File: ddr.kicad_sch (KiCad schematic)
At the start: 79 parts, among them U801 MT41K256M16TW

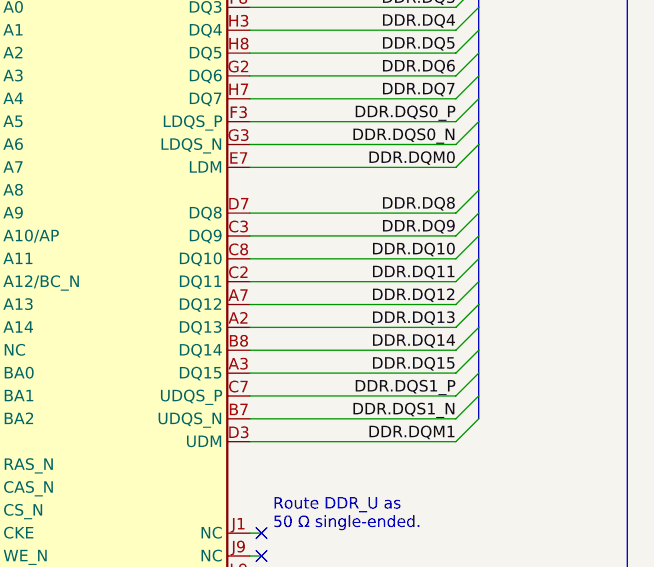
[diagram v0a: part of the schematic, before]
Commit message: Redo MPU fanout as dog-bone
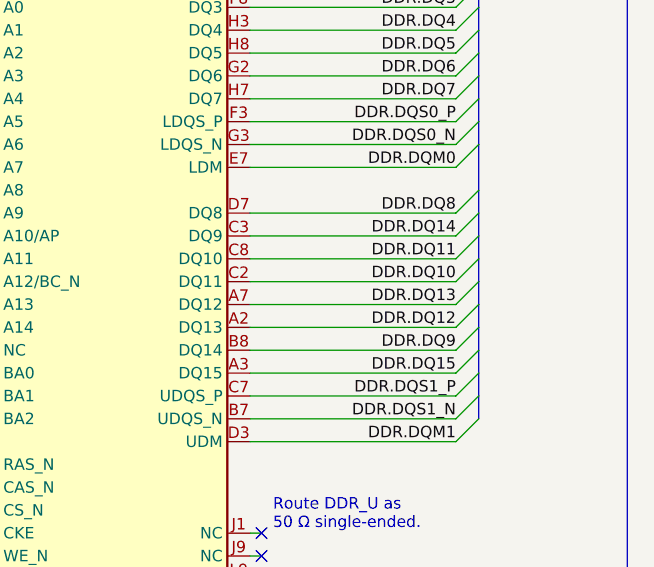
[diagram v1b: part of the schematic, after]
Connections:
- net DDR.DQ10: now also U801.C2 (DQ11); no longer U801.C8 (DQ10)
- net DDR.DQ11: now also U801.C8 (DQ10); no longer U801.C2 (DQ11)
- net DDR.DQ12: now also U801.A2 (DQ13); no longer U801.A7 (DQ12)
- net DDR.DQ13: now also U801.A7 (DQ12); no longer U801.A2 (DQ13)
- net DDR.DQ14: now also U801.C3 (DQ9); no longer U801.B8 (DQ14)
- net DDR.DQ9: now also U801.B8 (DQ14); no longer U801.C3 (DQ9)
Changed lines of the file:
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@@
 	)
 	(label "DDR.DQ13"
-		(at 387.35 142.24 180)
+		(at 387.35 139.7 180)
 		(effects
 			(font
@@
 	)
 	(label "DDR.DQ12"
-		(at 387.35 139.7 180)
+		(at 387.35 142.24 180)
 		(effects
 			(font
@@
 	)
 	(label "DDR.DQ14"
+		(at 387.35 132.08 180)
+		(effects
+			(font
+				(size 1.27 1.27)
+			)
+			(justify right bottom)
+		)
+	)
+	(label "DDR.DQ9"
 		(at 387.35 144.78 180)
-		(effects
-			(font
-				(size 1.27 1.27)
-			)
-			(justify right bottom)
-		)
-	)
-	(label "DDR.DQ9"
-		(at 387.35 132.08 180)
 		(effects
 			(font
@@
 	)
 	(label "DDR.DQ11"
-		(at 387.35 137.16 180)
+		(at 387.35 134.62 180)
 		(effects
 			(font
@@
 	)
 	(label "DDR.DQ10"
-		(at 387.35 134.62 180)
-		(effects
-			(font
+		(at 387.35 137.16 180)
+		(effects
+			(font

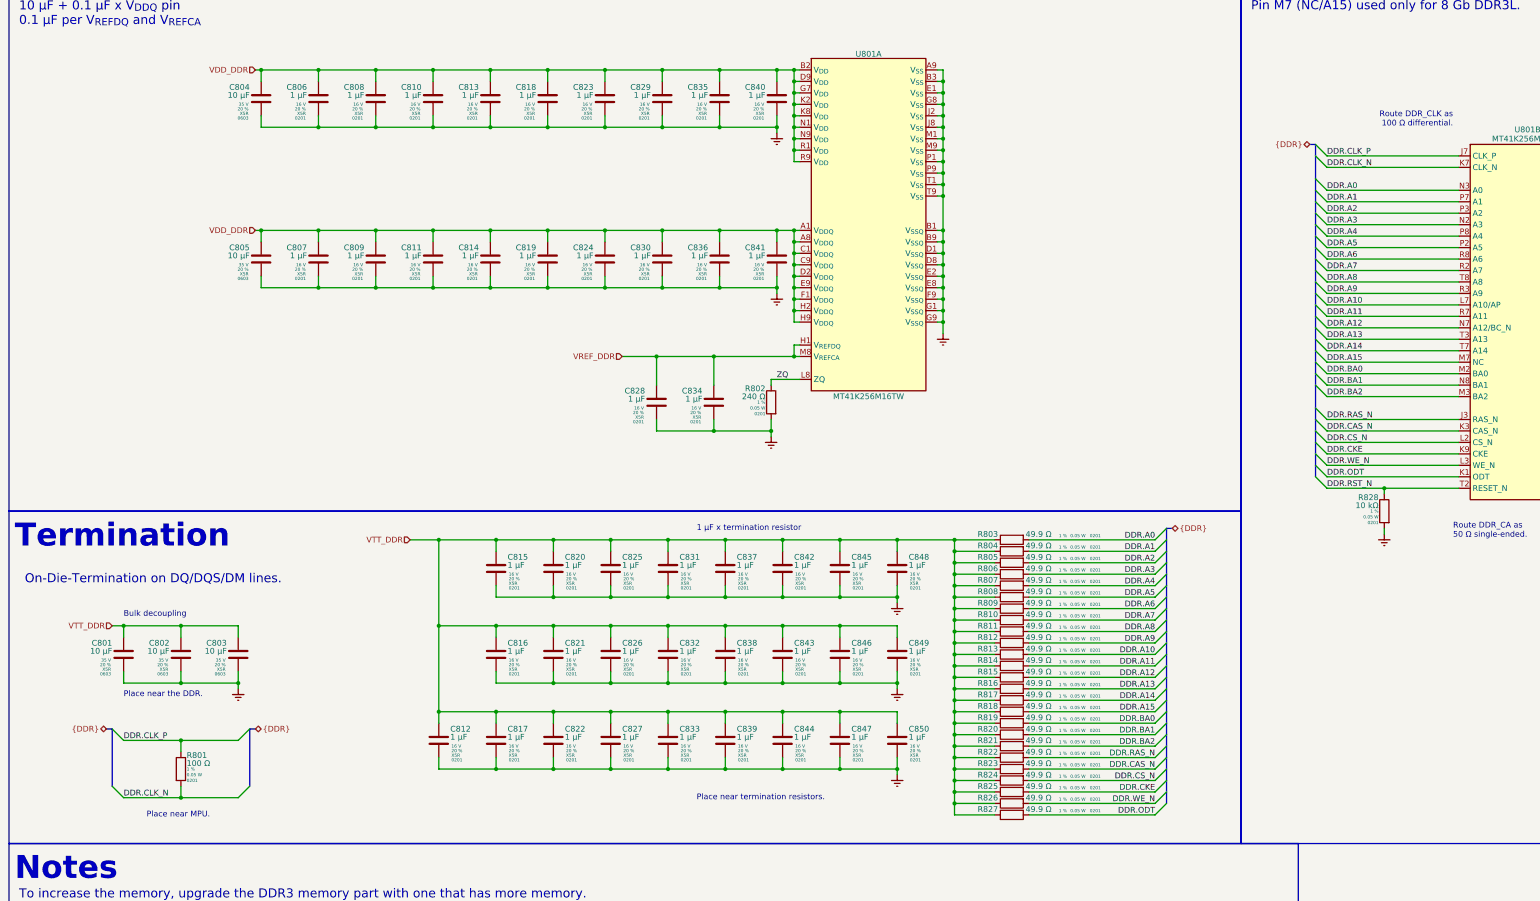
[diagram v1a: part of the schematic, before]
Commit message: Reorganize DDR termination
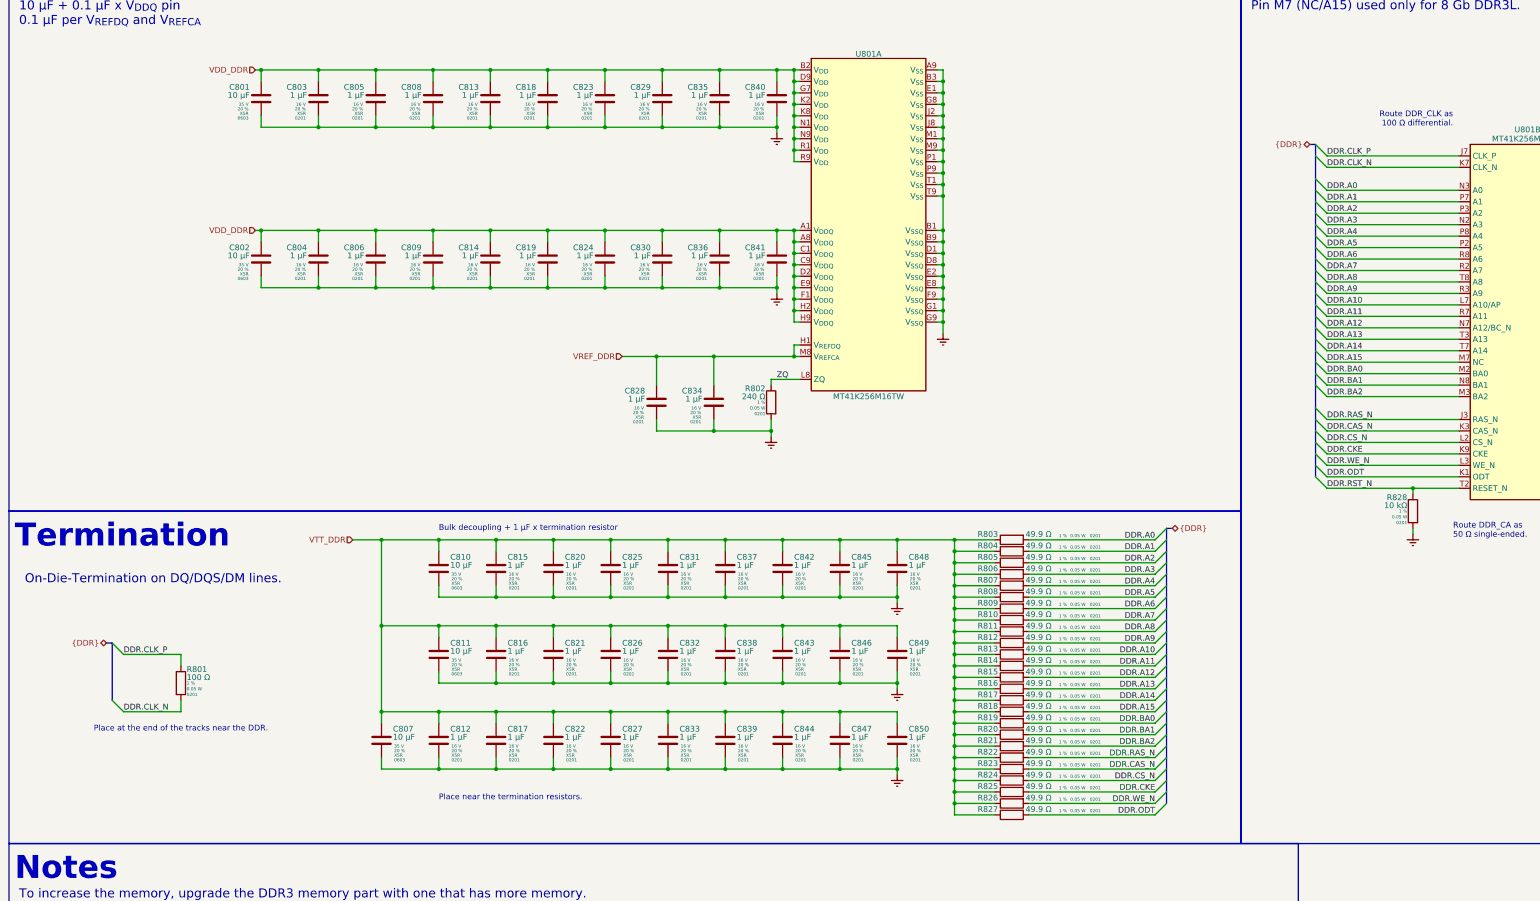
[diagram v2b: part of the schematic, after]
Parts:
- renumbered C804 to C801, C805 to C802, C806 to C803, C807 to C804, C808 to C805, C809 to C806, C803 to C807, C810 to C808, C811 to C809, C801 to C810, C802 to C811
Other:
- note added: "Bulk decoupling + 1 µF x termination resistor"
- note added: "Place at the end of the tracks near the DDR."
- note added: "Place near the termination resistors."
- note removed: "1 µF x termination resistor"
- note removed: "Bulk decoupling"
- note removed: "Place near MPU."
- note removed: "Place near termination resistors."
- note removed: "Place near the DDR."
- moved on the sheet: C807, C810, C811, R801, R828

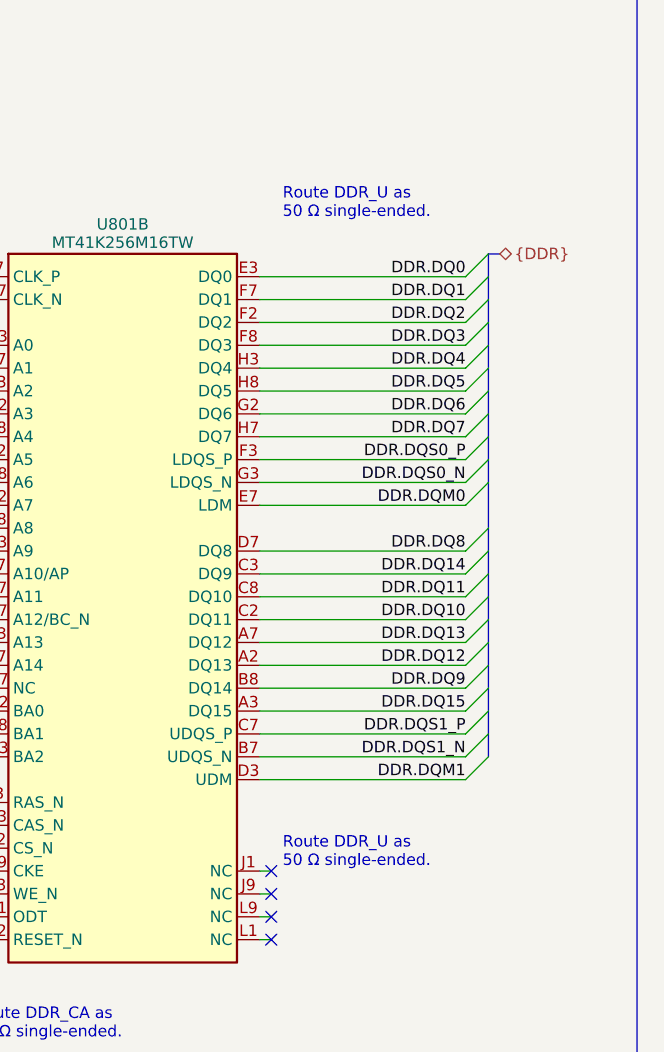
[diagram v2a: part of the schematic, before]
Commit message: DDR: Fix layout note
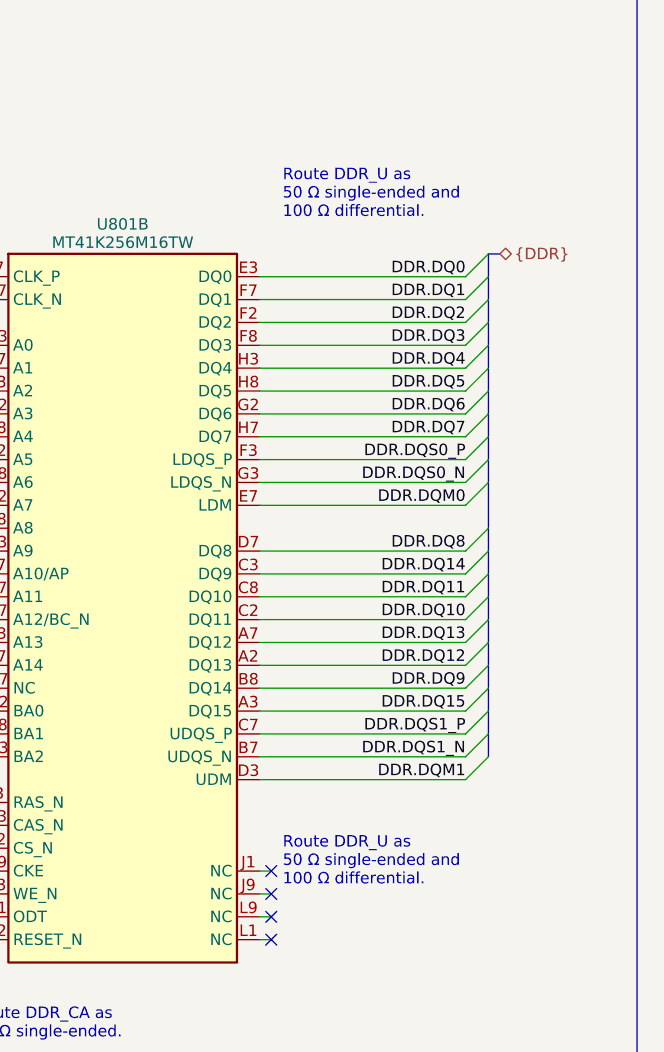
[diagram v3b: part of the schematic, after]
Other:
- note added: "Route DDR_U as 50 Ω single-ended and 100 Ω differential."
- note removed: "Route DDR_U as 50 Ω single-ended."
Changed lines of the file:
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@@
 		)
 	)
-	(text "Route DDR_U as\n50 Ω single-ended."
+	(text "Route DDR_U as\n50 Ω single-ended and\n100 Ω differential."
 		(exclude_from_sim no)
 		(at 367.03 161.29 0)
@@
 		)
 	)
-	(text "Route DDR_U as\n50 Ω single-ended."
+	(text "Route DDR_U as\n50 Ω single-ended and\n100 Ω differential."
 		(exclude_from_sim no)
 		(at 367.03 92.71 0)

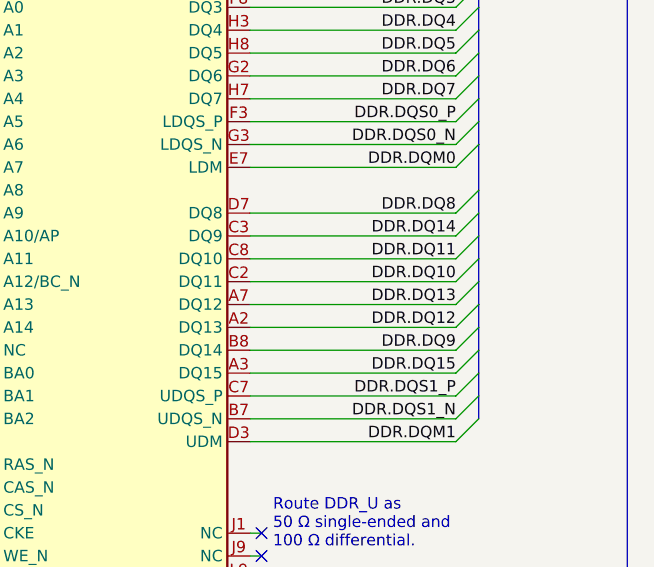
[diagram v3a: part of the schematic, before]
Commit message: Route the other DDR data lane
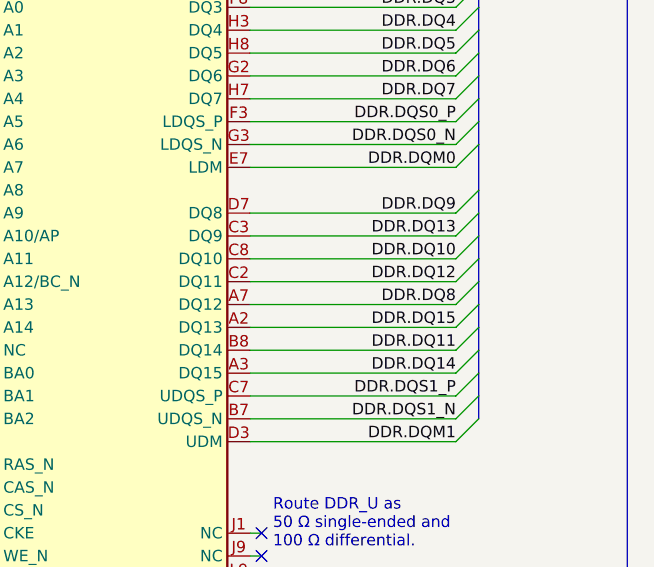
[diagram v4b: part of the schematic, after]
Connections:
- net DDR.DQ10: now also U801.C8 (DQ10); no longer U801.C2 (DQ11)
- net DDR.DQ11: now also U801.B8 (DQ14); no longer U801.C8 (DQ10)
- net DDR.DQ12: now also U801.C2 (DQ11); no longer U801.A2 (DQ13)
- net DDR.DQ13: now also U801.C3 (DQ9); no longer U801.A7 (DQ12)
- net DDR.DQ14: now also U801.A3 (DQ15); no longer U801.C3 (DQ9)
- net DDR.DQ15: now also U801.A2 (DQ13); no longer U801.A3 (DQ15)
- net DDR.DQ8: now also U801.A7 (DQ12); no longer U801.D7 (DQ8)
- net DDR.DQ9: now also U801.D7 (DQ8); no longer U801.B8 (DQ14)
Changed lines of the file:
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@@
 	)
 	(label "DDR.DQ13"
-		(at 387.35 139.7 180)
+		(at 387.35 132.08 180)
 		(effects
 			(font
@@
 	)
 	(label "DDR.DQ12"
-		(at 387.35 142.24 180)
+		(at 387.35 137.16 180)
 		(effects
 			(font
@@
 	)
 	(label "DDR.DQ14"
-		(at 387.35 132.08 180)
+		(at 387.35 147.32 180)
 		(effects
 			(font
@@
 	)
 	(label "DDR.DQ9"
-		(at 387.35 144.78 180)
+		(at 387.35 129.54 180)
 		(effects
 			(font
@@
 	)
 	(label "DDR.DQ11"
-		(at 387.35 134.62 180)
+		(at 387.35 144.78 180)
 		(effects
 			(font
@@
 	)
 	(label "DDR.DQ10"
-		(at 387.35 137.16 180)
+		(at 387.35 134.62 180)
 		(effects
 			(font
@@
 	)
 	(label "DDR.DQ15"
-		(at 387.35 147.32 180)
+		(at 387.35 142.24 180)
 		(effects
 			(font
@@
 	)
 	(label "DDR.DQ8"
-		(at 387.35 129.54 180)
-		(effects
-			(font
+		(at 387.35 139.7 180)
+		(effects
+			(font

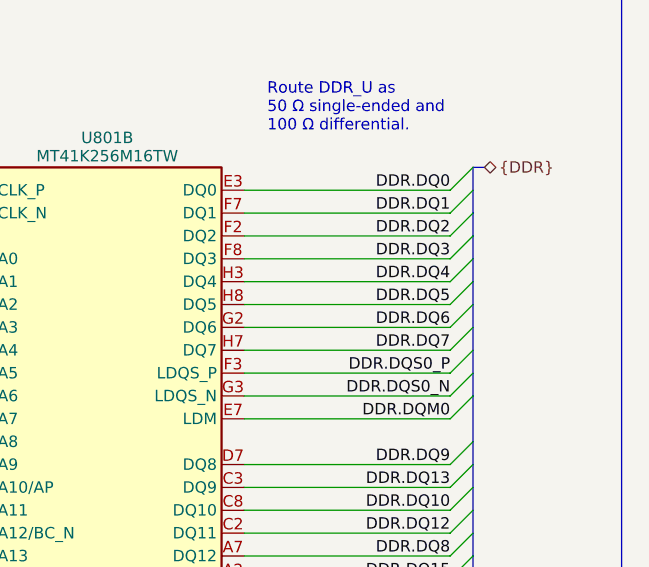
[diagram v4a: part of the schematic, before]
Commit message: Start re-routing DDR byte lanes
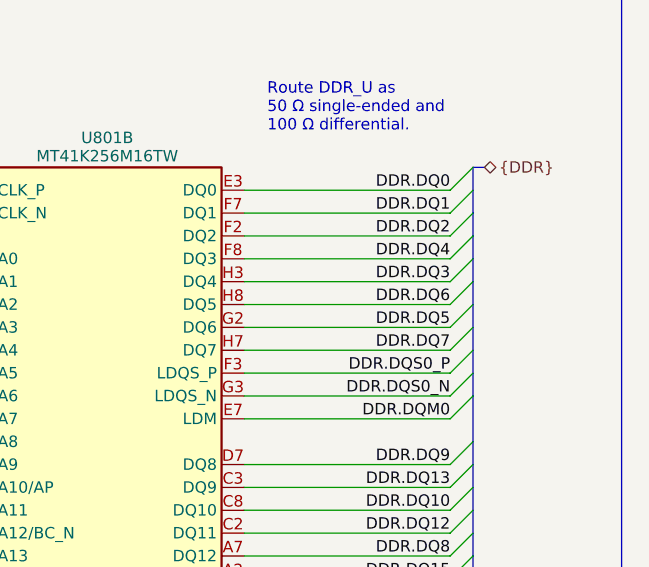
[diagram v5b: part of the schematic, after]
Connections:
- net DDR.DQ3: now also U801.H3 (DQ4); no longer U801.F8 (DQ3)
- net DDR.DQ4: now also U801.F8 (DQ3); no longer U801.H3 (DQ4)
- net DDR.DQ5: now also U801.G2 (DQ6); no longer U801.H8 (DQ5)
- net DDR.DQ6: now also U801.H8 (DQ5); no longer U801.G2 (DQ6)
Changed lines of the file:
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@@
 	)
 	(label "DDR.DQ6"
-		(at 387.35 114.3 180)
+		(at 387.35 111.76 180)
 		(effects
 			(font
@@
 	)
 	(label "DDR.DQ5"
-		(at 387.35 111.76 180)
+		(at 387.35 114.3 180)
 		(effects
 			(font
@@
 	)
 	(label "DDR.DQ4"
-		(at 387.35 109.22 180)
+		(at 387.35 106.68 180)
 		(effects
 			(font
@@
 	)
 	(label "DDR.DQ3"
-		(at 387.35 106.68 180)
-		(effects
-			(font
+		(at 387.35 109.22 180)
+		(effects
+			(font

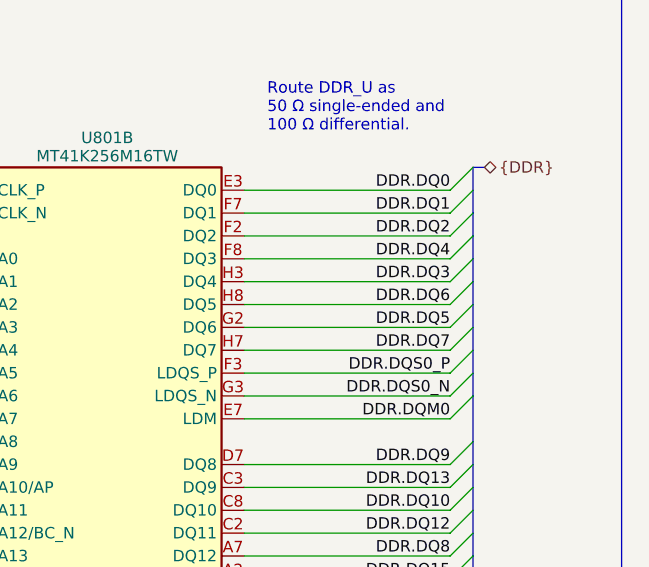
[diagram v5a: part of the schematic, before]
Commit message: Refine DDR routing
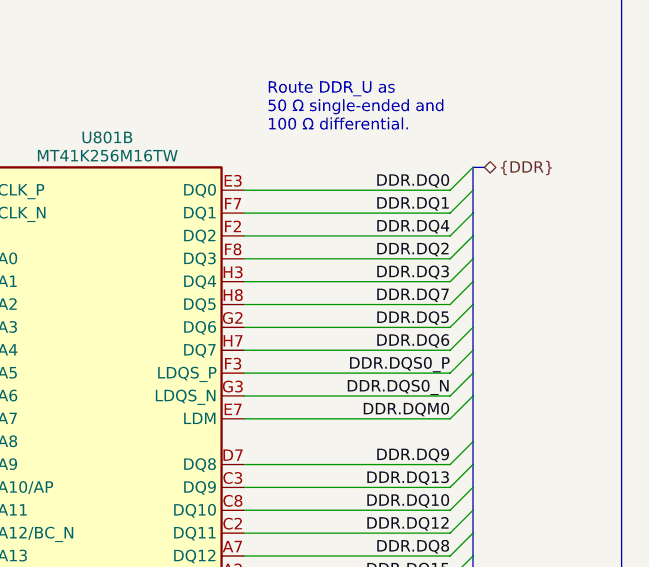
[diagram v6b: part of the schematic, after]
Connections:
- net DDR.DQ2: now also U801.F8 (DQ3); no longer U801.F2 (DQ2)
- net DDR.DQ4: now also U801.F2 (DQ2); no longer U801.F8 (DQ3)
- net DDR.DQ6: now also U801.H7 (DQ7); no longer U801.H8 (DQ5)
- net DDR.DQ7: now also U801.H8 (DQ5); no longer U801.H7 (DQ7)
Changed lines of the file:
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@@
 	)
 	(label "DDR.DQ6"
-		(at 387.35 111.76 180)
+		(at 387.35 116.84 180)
 		(effects
 			(font
@@
 	)
 	(label "DDR.DQ7"
-		(at 387.35 116.84 180)
+		(at 387.35 111.76 180)
 		(effects
 			(font
@@
 	)
 	(label "DDR.DQ4"
-		(at 387.35 106.68 180)
+		(at 387.35 104.14 180)
 		(effects
 			(font
@@
 	)
 	(label "DDR.DQ2"
-		(at 387.35 104.14 180)
-		(effects
-			(font
+		(at 387.35 106.68 180)
+		(effects
+			(font
